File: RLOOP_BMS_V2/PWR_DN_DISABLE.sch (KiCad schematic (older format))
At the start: 5 parts, among them Q1 FDN337N, U1 VOS618A-2X001T

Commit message: Footprint work
starting to assign footprints to parts
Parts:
- R5, R6, R7: footprint (none) -> Resistors_SMD:R_0603
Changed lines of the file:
@@
 F 0 "R6" V 5050 3050 50  0000 C CNN
 F 1 "270R / 0.1W / 5% / SMD 0603" H 5850 3050 50  0000 C CNN
-F 2 "" V 5080 3050 50  0001 C CNN
+F 2 "Resistors_SMD:R_0603" V 5080 3050 50  0001 C CNN
 F 3 "" H 5150 3050 50  0001 C CNN
 	1    5150 3050
@@
 F 0 "R7" V 6250 4150 50  0000 C CNN
 F 1 "2.2K / 0.1W / 1% / SMD 0603" H 7050 4150 50  0000 C CNN
-F 2 "" V 6280 4150 50  0001 C CNN
+F 2 "Resistors_SMD:R_0603" V 6280 4150 50  0001 C CNN
 F 3 "" H 6350 4150 50  0001 C CNN
 	1    6350 4150
@@
 F 0 "R5" V 4530 4150 50  0000 C CNN
 F 1 "1k" V 4450 4150 50  0000 C CNN
-F 2 "" V 4380 4150 50  0001 C CNN
+F 2 "Resistors_SMD:R_0603" V 4380 4150 50  0001 C CNN
 F 3 "" H 4450 4150 50  0001 C CNN
 	1    4450 4150

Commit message: footprint and layout work WIP
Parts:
- removed Q1: FDN337N, symbol Q_NMOS_DGS
- added Q1: FDN337N, TO_SOT_Packages_SMD:SOT-23, symbol Q_NMOS_GSD
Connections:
- net MCU_GND: now also Q1.2 (S)
- net at U1.2: now also Q1.3 (D)
- net at R5.1: now also Q1.1 (G)
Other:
- note removed: "CHECK PINOUT"
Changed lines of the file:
@@
-$EndComp
-$Comp
-L Q_NMOS_DGS Q1
-U 1 1 591384DA
-P 5050 4150
-F 0 "Q1" H 5250 4200 50  0000 L CNN
-F 1 "FDN337N" H 5250 4100 50  0000 L CNN
-F 2 "" H 5250 4250 50  0001 C CNN
-F 3 "" H 5050 4150 50  0001 C CNN
-	1    5050 4150
-	1    0    0    -1
 $EndComp
 $Comp
@@
 Wire Wire Line
 	5150 2650 5150 2900
-Text Notes 5250 4400 0    60   ~ 0
-CHECK PINOUT
 $Comp
 L LTV-814 U1
@@
 	1    0    0    -1
 $EndComp
+$Comp
+L Q_NMOS_GSD Q1
+U 1 1 5918AB93
+P 5050 4150
+F 0 "Q1" H 5250 4200 50  0000 L CNN
+F 1 "FDN337N" H 5250 4100 50  0000 L CNN
+F 2 "TO_SOT_Packages_SMD:SOT-23" H 5250 4250 50  0001 C CNN
+F 3 "" H 5050 4150 50  0001 C CNN
+	1    5050 4150
+	1    0    0    -1
+$EndComp

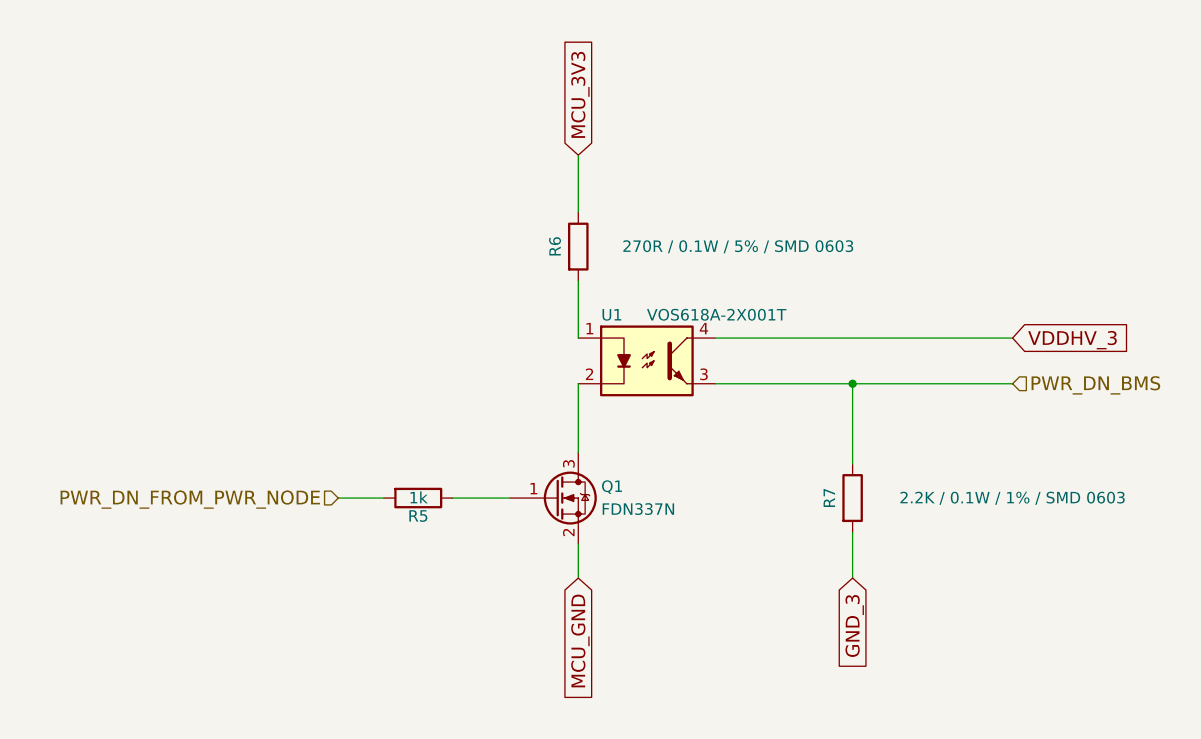
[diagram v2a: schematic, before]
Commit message: BMS v2 PCB work
almost done, mostly need to check stencil
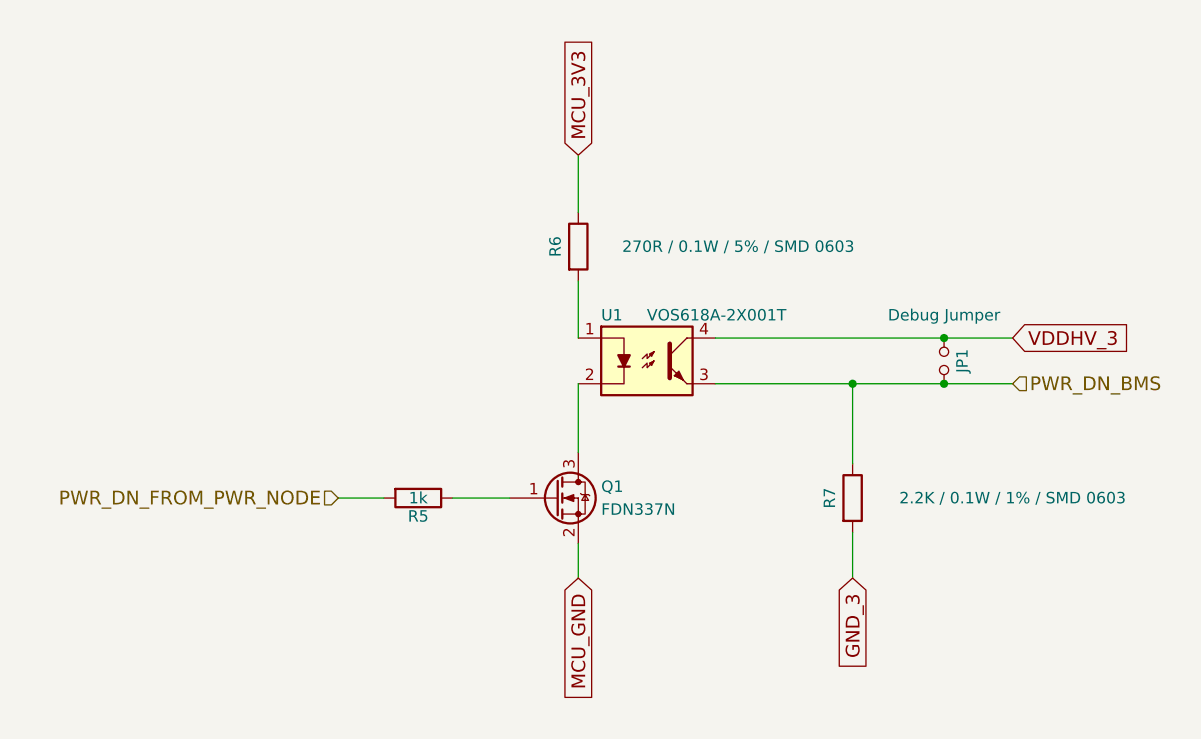
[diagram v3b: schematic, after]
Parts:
- added JP1: Debug Jumper, Pin_Headers:Pin_Header_Straight_1x02_Pitch2.54mm, symbol Jumper_NO_Small
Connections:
- net PWR_DN_BMS: now also JP1.2
- net VDDHV_3: now also JP1.1
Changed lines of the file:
@@
 	5150 3650 5150 3950
-Wire Wire Line
-	5750 3650 7050 3650
 Wire Wire Line
 	6350 4000 6350 3650
 Connection ~ 6350 3650
-Wire Wire Line
-	7050 3450 5750 3450
 Wire Wire Line
 	6350 4500 6350 4300
@@
 	1    0    0    -1
 $EndComp
+$Comp
+L Jumper_NO_Small JP1
+U 1 1 592244F5
+P 6750 3550
+F 0 "JP1" H 6750 3630 50  0000 C CNN
+F 1 "Debug Jumper" V 6550 3550 50  0000 C CNN
+F 2 "Pin_Headers:Pin_Header_Straight_1x02_Pitch2.54mm" H 6750 3550 50  0001 C CNN
+F 3 "" H 6750 3550 50  0001 C CNN
+	1    6750 3550
+	0    1    1    0
+$EndComp
+Wire Wire Line
+	5750 3450 7050 3450
+Wire Wire Line
+	5750 3650 7050 3650
+Connection ~ 6750 3650
+Connection ~ 6750 3450
 $EndSCHEMATC
